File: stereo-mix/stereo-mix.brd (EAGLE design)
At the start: 149.4 x 22.4 mm, 22 parts, among them IC3 LM324N

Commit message: gerber
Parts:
- removed C10, C9: 4.7u, rcl:PANASONIC_A
- removed D3, D4: 1N5819HW, diode:DO41-7.6
- removed GAIN1, GAIN2, GAIN3, GAIN4: 10k, MusicThingModular:DUAL_9MM_SNAP-IN_POT
- removed IC3: LM324N, linear:DIL14
- removed JP2: M05X2PTH, og-header:AVR_ICSP
- removed LEFT1, LEFT2, LEFT3, LEFT4, RIGHT1, RIGHT2, RIGHT3, RIGHT4, SUM_LEFT, SUM_RIGHT: THONKICONNNEW, MusicThingModular:WQP-PJ301M-12_JACK
- added D1, D2: (no value), diode:DO41-7.6
- added IC1: (no value), linear:DIL14
- added R1, R2: 1k, MusicThingModular:7MM_RESISTOR
- added R10, R3, R4, R7, R8, R9: 100k, MusicThingModular:7MM_RESISTOR
- added SV1: EURO_POWER_HEADERREGULAR, MusicThingModular:EURO_POWER_HEADER
- added U1, U10, U2, U3, U4, U5, U6, U7, U8, U9: THONKICONNNEW, MusicThingModular:WQP-PJ301M-12_JACK
- added VR1, VR2, VR3, VR4: 10k, MusicThingModular:DUAL_9MM_SNAP-IN_POT
- R5, R6: value 1k -> 100k; device MusicThingModular:10MM_RESISTOR -> MusicThingModular:7MM_RESISTOR
- moved R5 81.8 mm to (54.6, 5.84)
- moved R6 76.7 mm to (54.6, 16.8), turned to 270 degrees
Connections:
- removed net N$23: D4.A, JP2.1, JP2.2
- removed net N$24: D3.C, JP2.10, JP2.9
- removed net N$26: LEFT1.P$2_SWITCH, RIGHT1.P$1_TIP
- removed net N$30: GAIN1.3B, RIGHT1.P$2_SWITCH
- removed net N$34: LEFT2.P$2_SWITCH, RIGHT2.P$1_TIP
- removed net N$35: GAIN2.3, LEFT2.P$1_TIP
- removed net N$36: GAIN2.3B, RIGHT2.P$2_SWITCH
- removed net N$39: LEFT3.P$2_SWITCH, RIGHT3.P$1_TIP
- removed net N$41: GAIN3.3B, RIGHT3.P$2_SWITCH
- removed net N$44: LEFT4.P$2_SWITCH, RIGHT4.P$1_TIP
- removed net N$46: GAIN4.3B, RIGHT4.P$2_SWITCH
- new net N$1: R4.2, VR1.2B
- new net N$10: D2.C, SV1.2
- new net N$11: U4.P$1_TIP, VR1.3B
- new net N$12: U5.P$1_TIP, U6.P$2_SWITCH, VR2.3
- new net N$13: U6.P$1_TIP, VR2.3B
- new net N$14: D1.A, SV1.10
- new net N$15: U8.P$1_TIP, VR3.3B
- new net N$18: U10.P$1_TIP, VR4.3B
- new net N$2: R3.2, VR1.2
- new net N$3: R5.2, VR2.2
- new net N$4: R6.2, VR2.2B
- new net N$5: R7.2, VR3.2
- new net N$7: R8.2, VR3.2B
- new net N$8: R9.2, VR4.2
- new net N$9: R10.2, VR4.2B
- net GND: now also SV1.3, SV1.5, SV1.7, U1.P$3_SLEEVE, U10.P$3_SLEEVE, U2.P$3_SLEEVE, U3.P$3_SLEEVE, U4.P$3_SLEEVE, U5.P$3_SLEEVE, U6.P$3_SLEEVE, U7.P$3_SLEEVE, U8.P$3_SLEEVE, U9.P$3_SLEEVE, VR1.1, VR1.1B, VR2.1, VR2.1B, VR3.1, VR3.1B, VR4.1, VR4.1B; no longer C10.+, C9.-, JP2.3, JP2.4, JP2.5, JP2.6, JP2.7, JP2.8, LEFT1.P$3_SLEEVE, LEFT2.P$3_SLEEVE, LEFT3.P$3_SLEEVE, LEFT4.P$3_SLEEVE, RIGHT1.P$3_SLEEVE, RIGHT2.P$3_SLEEVE, RIGHT3.P$3_SLEEVE, RIGHT4.P$3_SLEEVE, SUM_LEFT.P$3_SLEEVE, SUM_RIGHT.P$3_SLEEVE
- net N$20: now also R2.1, U3.P$1_TIP; no longer R6.1, SUM_RIGHT.P$1_TIP
- net N$25: now also U2.P$1_TIP, U4.P$2_SWITCH, VR1.3; no longer GAIN1.3, LEFT1.P$1_TIP
- net N$27: now also IC1.6, IC1.7, R2.2; no longer IC3.6, IC3.7, R6.2
- net N$29: now also IC1.1, IC1.2, R1.2; no longer IC3.1, IC3.2, R5.2
- net N$40: now also U7.P$1_TIP, U8.P$2_SWITCH, VR3.3; no longer GAIN3.3, LEFT3.P$1_TIP
- net N$45: now also U10.P$2_SWITCH, U9.P$1_TIP, VR4.3; no longer GAIN4.3, LEFT4.P$1_TIP
- net N$47: now also IC1.3, R3.1, R5.1, R7.1, R9.1; no longer GAIN1.2, GAIN2.2, GAIN3.2, GAIN4.2, IC3.3
- net N$48: now also IC1.5, R10.1, R4.1, R6.1, R8.1; no longer GAIN1.2B, GAIN2.2B, GAIN3.2B, GAIN4.2B, IC3.5
- net N$6: now also R1.1, U1.P$1_TIP; no longer R5.1, SUM_LEFT.P$1_TIP
- net VCC: now also D1.C, IC1.4; no longer C9.+, D4.C, IC3.4
- net VEE: now also D2.A, IC1.11; no longer C10.-, D3.A, IC3.11
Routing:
- net VEE: track 75.7 -> 34.5 mm, vias 1 -> 0
- net N$12: track 0.00 -> 28.4 mm
- net N$35: track 26.7 -> 0.00 mm, vias 1 -> 0
- net N$18: track 0.00 -> 24.6 mm
- net N$13: track 0.00 -> 24.0 mm
- net N$15: track 0.00 -> 23.8 mm
- net N$29: track 31.3 -> 8.44 mm
- net N$11: track 0.00 -> 22.7 mm
- net VCC: track 44.4 -> 22.1 mm, vias 1 -> 0
- net N$23: track 19.0 -> 0.00 mm
- net N$24: track 17.9 -> 0.00 mm
- net N$6: track 20.9 -> 5.11 mm
- net N$27: track 22.2 -> 6.77 mm
- net N$41: track 14.7 -> 0.00 mm, vias 1 -> 0
- net N$36: track 14.4 -> 0.00 mm, vias 1 -> 0
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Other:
- board text added: "2018"
- board text added: "Paul Adenot"
- board text added: "stereo mixer 0.0.1"

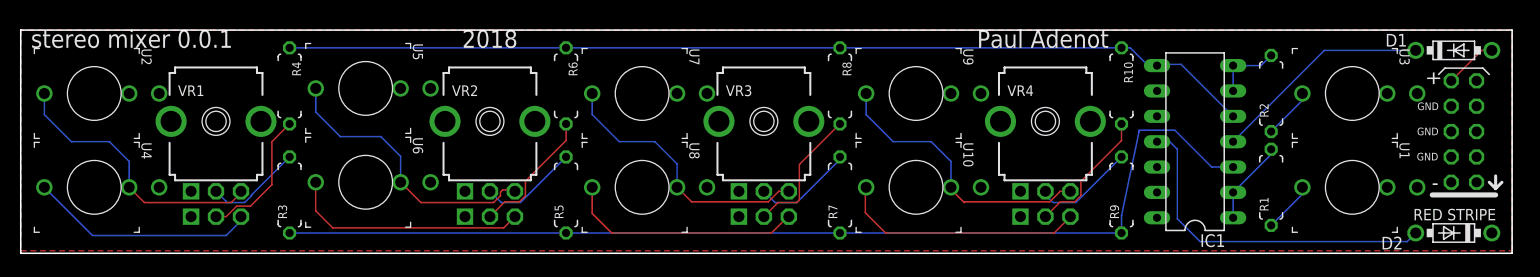
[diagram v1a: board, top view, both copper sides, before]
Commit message: update stereo-mix 0.0.2
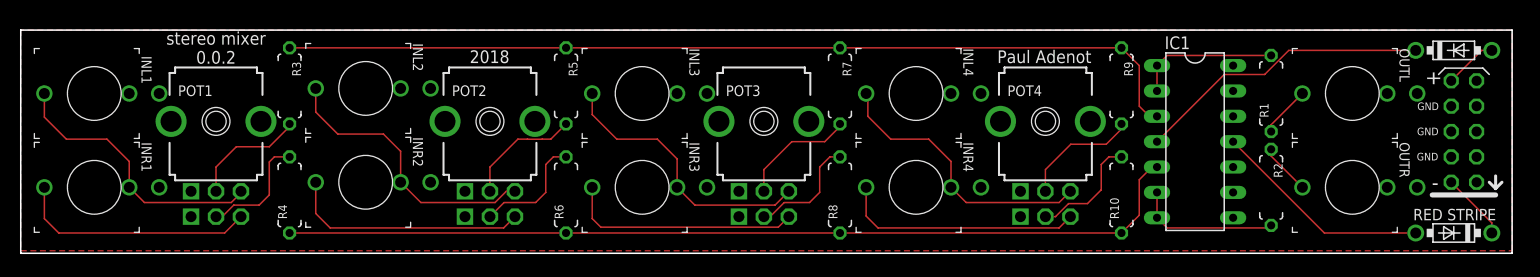
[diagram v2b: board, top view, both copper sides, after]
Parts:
- R10, R3, R4, R5, R6, R7, R8, R9: value 100k -> 1k
- moved R10 10.9 mm to (110.2, 5.84), turned to 90 degrees
- moved R3 10.9 mm to (26.9, 16.8), turned to 270 degrees
- moved R4 10.9 mm to (26.9, 5.84), turned to 90 degrees
- moved R5 10.9 mm to (54.6, 16.8), turned to 270 degrees
- moved R6 10.9 mm to (54.6, 5.84), turned to 90 degrees
- moved R7 10.9 mm to (82.0, 16.8), turned to 270 degrees
- moved R8 10.9 mm to (82.0, 5.84), turned to 90 degrees
- moved R9 10.9 mm to (110.2, 16.8), turned to 270 degrees
- moved R1 9.40 mm to (125.2, 16.0)
- moved R2 9.40 mm to (125.2, 6.60), turned to 270 degrees
- turned IC1 to 270 degrees
- renumbered U1 to OUTR, U10 to INR4, U2 to INL1, U3 to OUTL, U4 to INR1, U5 to INL2, U6 to INR2, U7 to INL3, U8 to INR3, U9 to INL4, VR1 to POT1, VR2 to POT2, VR3 to POT3, VR4 to POT4
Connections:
- net N$20: now also OUTR.P$1_TIP; no longer OUTL.P$1_TIP
- net N$6: now also OUTL.P$1_TIP; no longer OUTR.P$1_TIP
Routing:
- net N$47: track 104.7 -> 92.1 mm
- net VEE: track 34.5 -> 22.1 mm
- net N$27: track 6.77 -> 14.5 mm
- net VCC: track 22.1 -> 29.7 mm
- net N$10: track 0.00 -> 6.76 mm
- net N$29: track 8.44 -> 14.4 mm
- net N$48: track 97.3 -> 91.7 mm
- net N$1: track 13.7 -> 11.8 mm
- net N$7: track 13.5 -> 11.6 mm
- net N$2: track 9.83 -> 11.7 mm
- net N$3: track 9.98 -> 11.8 mm
- net N$8: track 10.2 -> 12.0 mm
- net N$5: track 10.1 -> 11.8 mm
- net N$9: track 13.3 -> 11.6 mm
- net N$4: track 13.3 -> 11.7 mm
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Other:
- board text added: "stereo mixer 0.0.2"
- board text removed: "stereo mixer 0.0.1"
